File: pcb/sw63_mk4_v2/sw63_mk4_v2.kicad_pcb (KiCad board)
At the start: 4 copper layers, 35.1 x 36 mm, 70 parts, among them J1 GT-USB-7070C, J2 SWD, J3 Conn_01x02, Q1 DMG2305UX-7, Q2 DMG2302U-7, Q3 TEMT6200FX01, SW1 KSC321J LFS, SW2 ﻿EVQ-P7J01P, U1 DIO5518BST5, U2 MCP1711T-3.3I/OT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

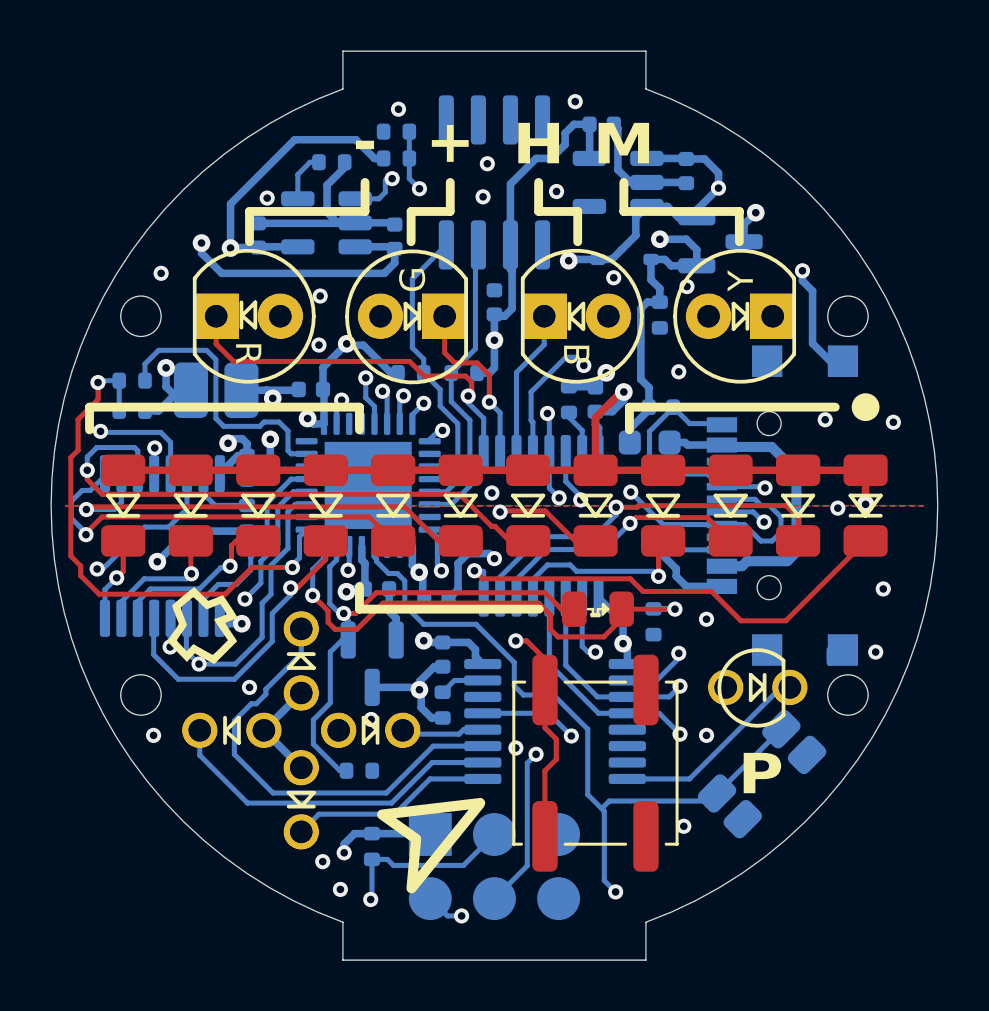
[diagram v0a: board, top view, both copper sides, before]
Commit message: slightly smaller pcb, better fit in the enclosure
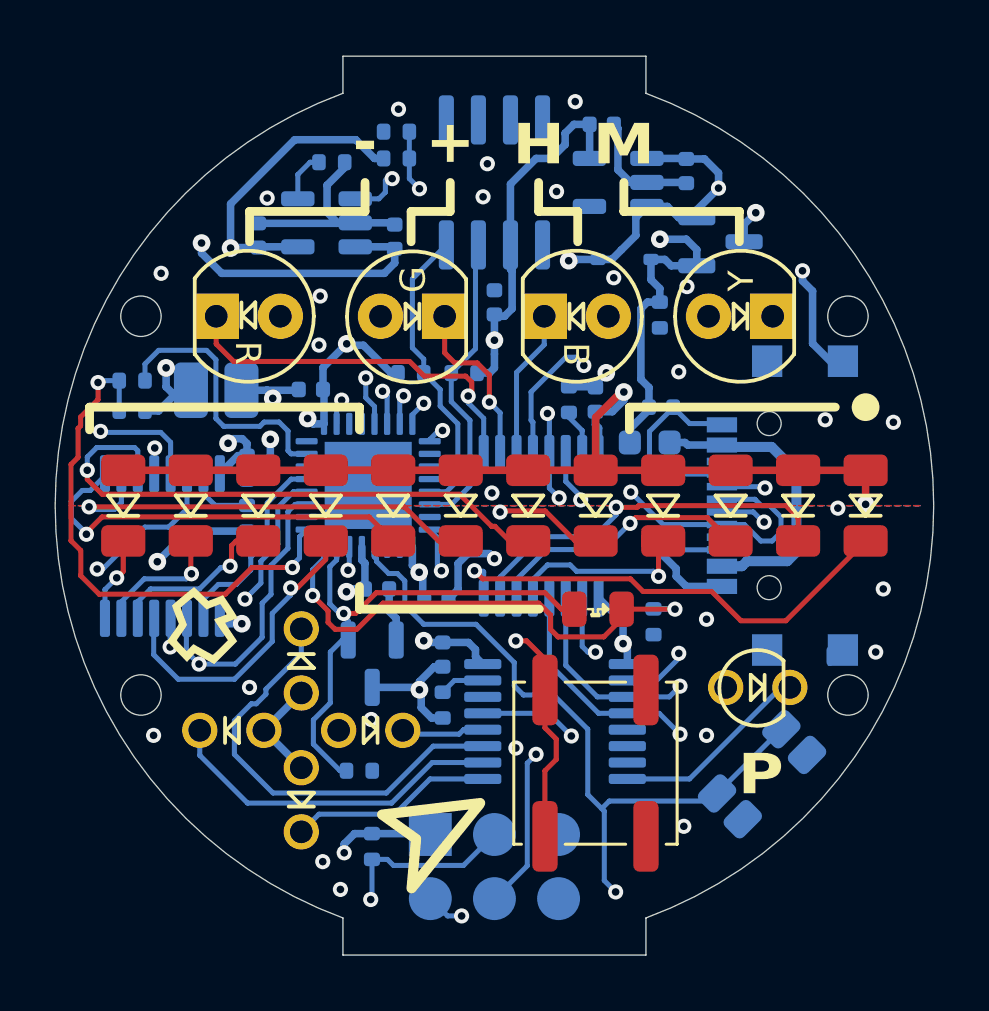
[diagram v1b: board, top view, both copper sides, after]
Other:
- board size 35.1 x 36 mm -> 34.8 x 35.6 mm
- board text added: "CK"
- board text added: "DT"
- board text added: "G"
- board text added: "NC"
- board text added: "R"
- board text added: "V"
